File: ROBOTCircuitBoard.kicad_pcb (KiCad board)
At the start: 2 copper layers, 52.1 x 74.9 mm, 13 parts, among them J1 DB15_HighDensity_MountingHoles, J2 DB15_HighDensity_MountingHoles, P1 CONN_01X03, P2 CONN_01X04, P3 CONN_01X04, P4 CONN_01X04, U1 MCP2551-I/P, U2 Teensy3.2

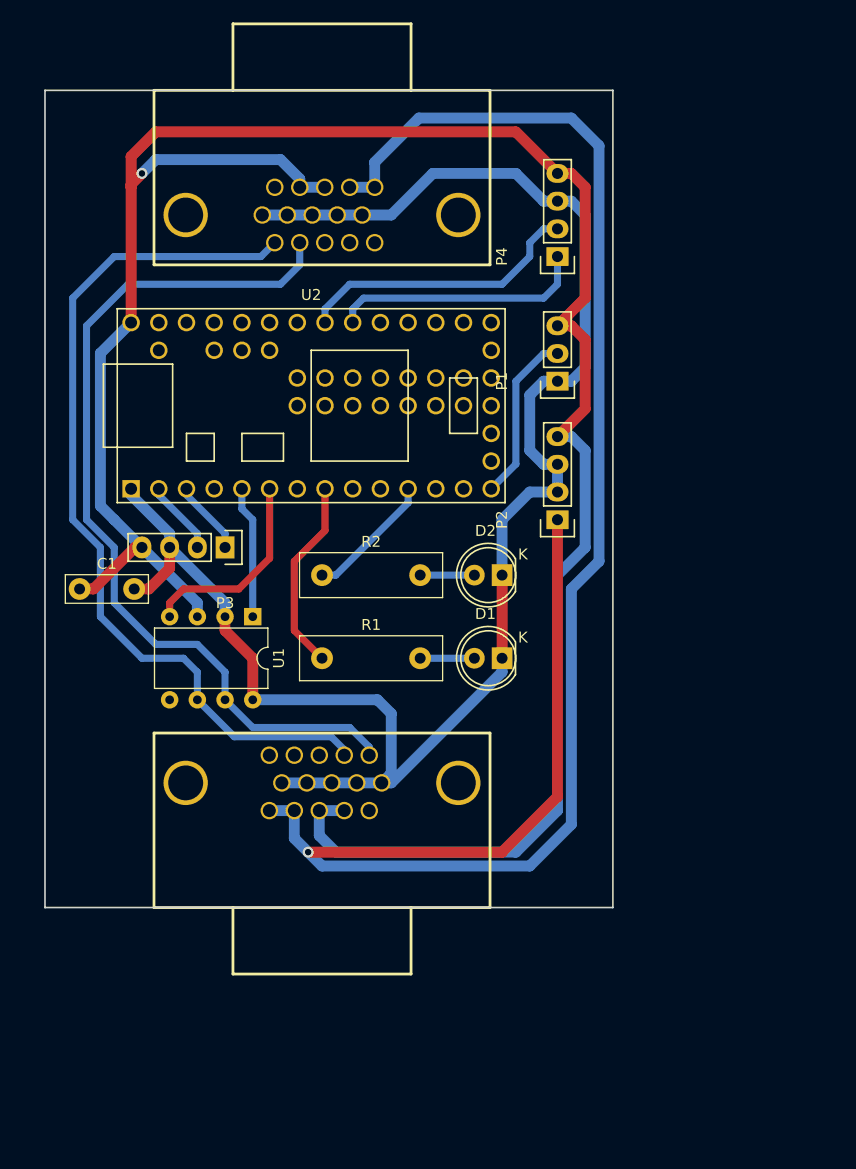
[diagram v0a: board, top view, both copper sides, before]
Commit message: Added four pin connectors, 5V layer, GND layer, and other misceallaneous jobs.
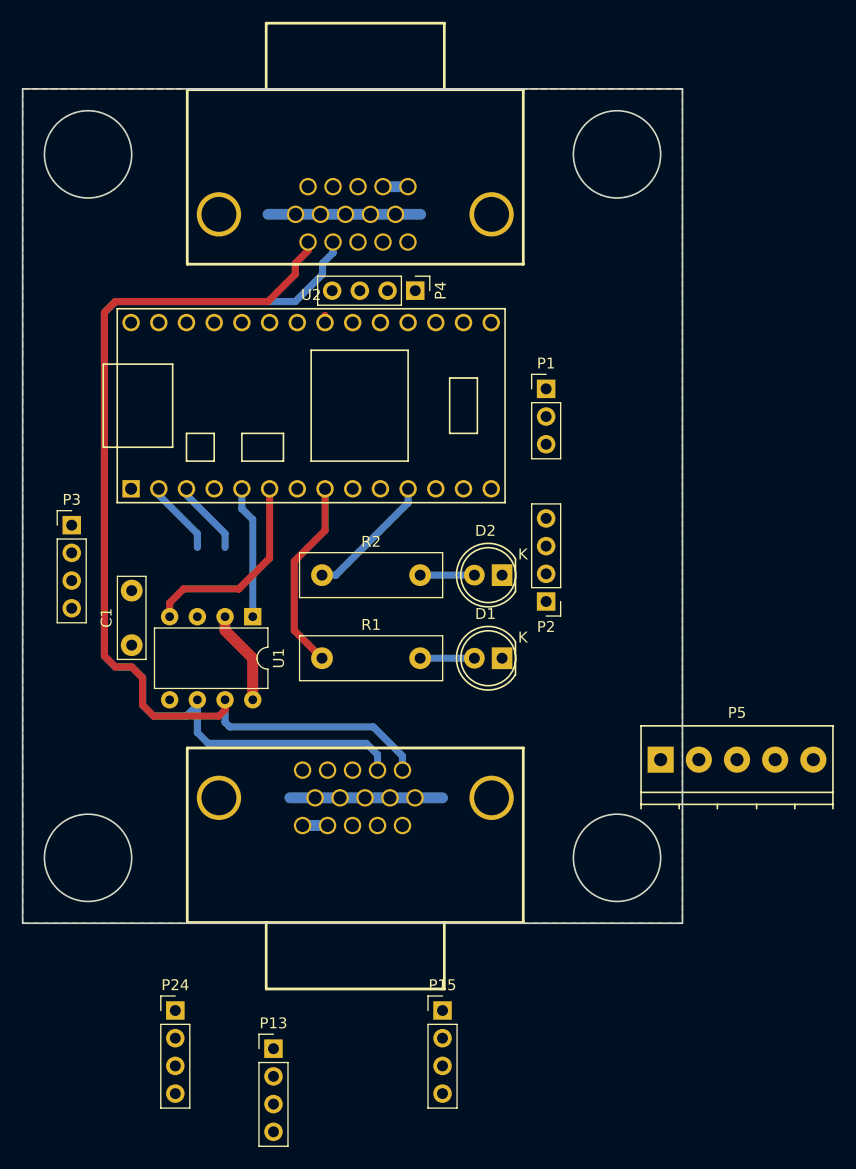
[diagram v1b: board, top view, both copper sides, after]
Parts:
- added P13: CONN_01X04, Socket_Strips:Socket_Strip_Straight_1x04_Pitch2.54mm, F.Cu at (167.0, 175.5)
- added P15: CONN_01X04, Socket_Strips:Socket_Strip_Straight_1x04_Pitch2.54mm, F.Cu at (182.5, 172.0)
- added P24: CONN_01X04, Socket_Strips:Socket_Strip_Straight_1x04_Pitch2.54mm, F.Cu at (158.0, 172.0)
- added P5: CONN_01X05, Connectors_Terminal_Blocks:TerminalBlock_Pheonix_PT-3.5mm_5pol, F.Cu at (202.5, 149.0)
- P1: footprint Socket_Strips:Socket_Strip_Straight_1x03 -> Socket_Strips:Socket_Strip_Straight_1x03_Pitch2.54mm
- P2, P3, P4: footprint Socket_Strips:Socket_Strip_Straight_1x04 -> Socket_Strips:Socket_Strip_Straight_1x04_Pitch2.54mm
- U2: footprint Teensy:Teensy30_31_32_LC -> Teensy:Teensy30_31_32_LC_LessPins
- moved P3 14.2 mm to (148.5, 127.5), turned to 0 degrees
- moved P4 13.4 mm to (180.0, 106.0), turned to 270 degrees
- moved P2 7.57 mm to (192.0, 134.5), turned to 180 degrees
- moved C1 7.02 mm to (154.0, 138.5), turned to 90 degrees
- moved J1 3.34 mm to (174.5, 152.5)
- moved J2 3.05 mm to (174.5, 99.0)
- moved P1 1.25 mm to (192.0, 115.0), turned to 0 degrees
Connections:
- J2 pad 1: /CANL -> /CANH
- J2 pad 2: /CANH -> /CANL
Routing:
- net +5V: track 212.0 -> 0.02 mm, vias 1 -> 0
- net +12V: track 174.6 -> 4.58 mm, vias 1 -> 0
- net GND: track 157.9 -> 36.7 mm
- net /1B: track 26.4 -> 0.67 mm
- net /1A: track 23.5 -> 0.00 mm
- net /DIN: track 15.7 -> 0.00 mm
- net /CANL: track 80.3 -> 91.2 mm
- net /CANH: track 81.4 -> 90.8 mm
- net Net-(J1-Pad0): track 1.47 -> 0.00 mm
- added copper zone on F.Cu, net +5V
- added copper zone on B.Cu, net GND
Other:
- board size 52.1 x 74.9 mm -> 60.5 x 76.5 mm

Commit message: added some 5v GND DATA DATA ports. Repositioned Pololu. Reduced board size slightly
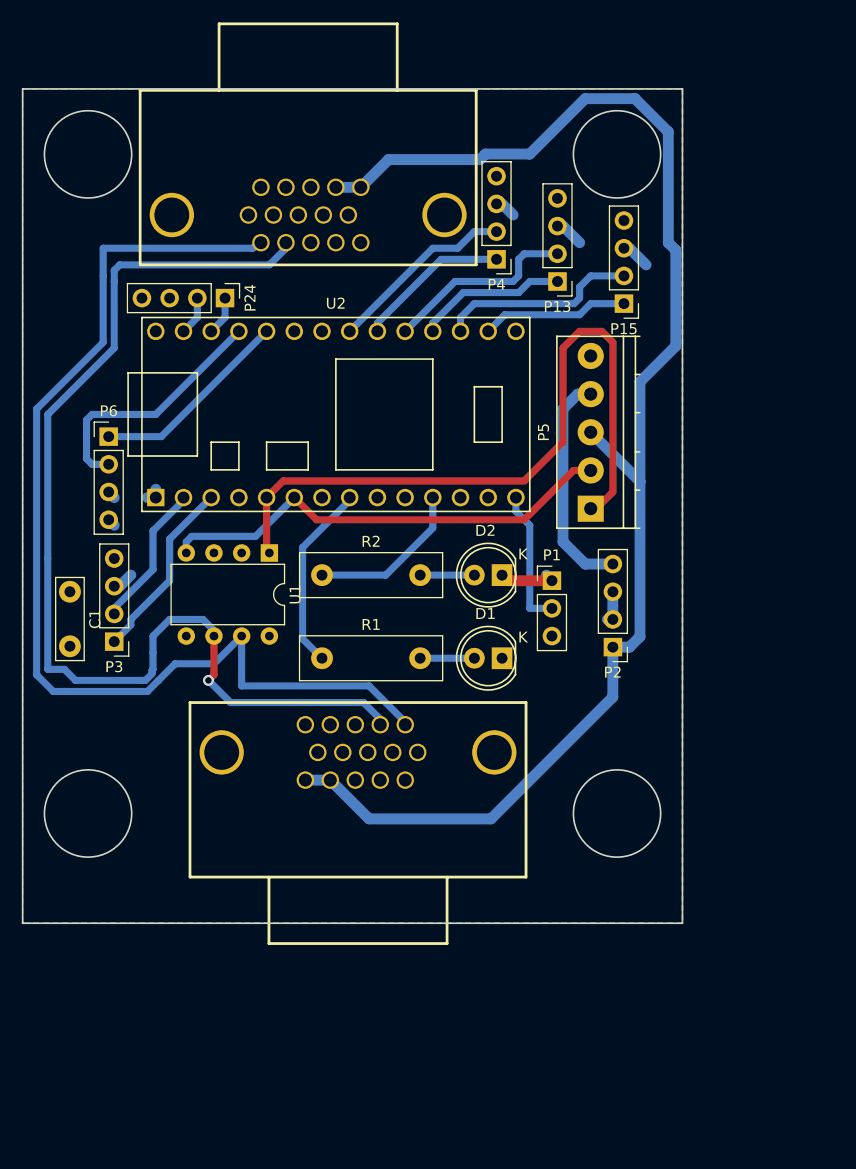
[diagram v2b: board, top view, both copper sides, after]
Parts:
- added P6: CONN_01X04, Socket_Strips:Socket_Strip_Straight_1x04_Pitch2.54mm, F.Cu at (151.9, 119.4)
- moved P13 75.0 mm to (193.0, 105.2), turned to 180 degrees
- moved P15 66.9 mm to (199.1, 107.2), turned to 180 degrees
- moved P24 65.5 mm to (162.6, 106.7), turned to 270 degrees
- moved P5 23.9 mm to (196.1, 126.0), turned to 90 degrees
- moved P1 17.6 mm to (192.5, 132.6)
- moved P3 11.4 mm to (152.4, 138.2), turned to 180 degrees
- moved P4 7.99 mm to (187.5, 103.1), turned to 180 degrees
- moved C1 7.49 mm to (148.3, 133.6), turned to 270 degrees
- moved P2 7.41 mm to (198.1, 138.7)
- moved U1 6.04 mm to (166.6, 130.0)
- moved J2 4.32 mm to (170.2, 99.1)
- moved J1 4.17 mm to (174.8, 148.3)
- moved U2 2.40 mm to (172.7, 117.3)
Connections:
- net Net-(U2-Pad27) renamed /A4
- net Net-(U2-Pad28) renamed /A5
- P13 pad 1: Net-(P13-Pad1) -> /A2
- P13 pad 2: Net-(P13-Pad2) -> /A3
- P13 pad 3: Net-(P13-Pad3) -> GND
- P13 pad 4: Net-(P13-Pad4) -> +5V
- P15 pad 1: Net-(P15-Pad1) -> /A0
- P15 pad 2: Net-(P15-Pad2) -> /A1
- P15 pad 3: Net-(P15-Pad3) -> GND
- P15 pad 4: Net-(P15-Pad4) -> +5V
- P24 pad 1: Net-(P24-Pad1) -> /A8
- P24 pad 2: Net-(P24-Pad2) -> /A9
- P24 pad 3: Net-(P24-Pad3) -> GND
- P24 pad 4: Net-(P24-Pad4) -> +5V
- P5 pad 1: Net-(P5-Pad1) -> /CAN_Tx
- P5 pad 2: Net-(P5-Pad2) -> /CAN_Rx
- P5 pad 3: Net-(P5-Pad3) -> +12V
- P5 pad 4: Net-(P5-Pad4) -> +5V
- P5 pad 5: Net-(P5-Pad5) -> GND
- U2 pad 21: Net-(U2-Pad21) -> /A0
- U2 pad 22: Net-(U2-Pad22) -> /A1
- U2 pad 23: Net-(U2-Pad23) -> /A2
- U2 pad 24: Net-(U2-Pad24) -> /A3
- U2 pad 29: Net-(U2-Pad29) -> /A6
- U2 pad 30: Net-(U2-Pad30) -> /A7
- U2 pad 31: Net-(U2-Pad31) -> /A8
- U2 pad 32: Net-(U2-Pad32) -> /A9
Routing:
- net +12V: track 4.58 -> 131.2 mm
- net /CAN_Tx: track 12.1 -> 65.1 mm
- net /CAN_Rx: track 18.5 -> 42.5 mm
- net /A7: track 0.00 -> 23.1 mm
- net +5V: track 0.02 -> 22.1 mm
- net /A6: track 0.00 -> 18.5 mm
- net /A1: track 0.00 -> 18.4 mm
- net /A3: track 0.00 -> 17.8 mm
- net /1B: track 0.67 -> 17.2 mm
- net GND: track 36.7 -> 20.9 mm
- net /1A: track 0.00 -> 14.1 mm
- net /A2: track 0.00 -> 13.8 mm
- net /A0: track 0.00 -> 13.5 mm
- net /DIN: track 0.00 -> 12.7 mm
- net /0B: track 6.84 -> 16.9 mm
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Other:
- outline, holes or cut-outs redrawn

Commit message: fixed board size
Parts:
- moved J1 4.06 mm to (174.8, 152.4)
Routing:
- net /CANL: track 99.1 -> 103.1 mm
- net /CANH: track 99.3 -> 103.4 mm
- net +12V: track 131.2 -> 134.3 mm
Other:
- outline, holes or cut-outs redrawn
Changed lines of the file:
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@@
     (links 72)
     (no_connects 2)
-    (area 143.924999 87.424999 204.575001 164.075001)
+    (area 143.924999 81.206999 204.592004 166.189001)
     (thickness 1.6)
     (drawings 8)
-    (tracks 180)
+    (tracks 183)
     (zones 0)
     (modules 18)
@@
   )
   (module conn-db15-SPC15430:conn_SPC15430 (layer F.Cu)
-    (at 174.752 148.336 180)
+    (at 174.752 152.4 180)
     (fp_text reference J1 (at -8.6487 -6.9088 180) (layer F.SilkS) hide
       (effects (font (size 0.59944 0.59944) (thickness 0.0508)))
@@
   (gr_line (start 204.5 164) (end 144 164) (angle 90) (layer Edge.Cuts) (width 0.15))
   (gr_line (start 204.5 87.5) (end 204.5 164) (angle 90) (layer Edge.Cuts) (width 0.15))
-  (gr_circle (center 150 153.936) (end 154 153.936) (layer Edge.Cuts) (width 0.15))
-  (gr_circle (center 198.5 153.936) (end 194.5 153.936) (layer Edge.Cuts) (width 0.15))
+  (gr_circle (center 149.492 157.492) (end 153.492 157.492) (layer Edge.Cuts) (width 0.15))
+  (gr_circle (center 198.5 158) (end 194.5 158) (layer Edge.Cuts) (width 0.15))
   (gr_circle (center 198.5 93.5) (end 194.5 93.5) (layer Edge.Cuts) (width 0.15))
   (gr_circle (center 150 93.5) (end 154 93.5) (layer Edge.Cuts) (width 0.15))
@@
   (segment (start 180.45 139.7) (end 185.42 139.7) (width 0.65) (layer B.Cu) (net 2))
   (segment (start 180.45 132.08) (end 185.42 132.08) (width 0.65) (layer B.Cu) (net 3))
-  (segment (start 198.12 138.684) (end 198.12 143.256) (width 1) (layer B.Cu) (net 5))
-  (segment (start 175.768 154.432) (end 172.212 150.876) (width 1) (layer B.Cu) (net 5))
-  (segment (start 186.944 154.432) (end 175.768 154.432) (width 1) (layer B.Cu) (net 5))
-  (segment (start 198.12 143.256) (end 186.944 154.432) (width 1) (layer B.Cu) (net 5))
-  (segment (start 169.922 150.876) (end 172.212 150.876) (width 1) (layer B.Cu) (net 5))
+  (segment (start 172.212 154.94) (end 172.212 155.956) (width 1) (layer B.Cu) (net 5) (status 400000))
+  (segment (start 198.12 146.812) (end 198.12 138.684) (width 1) (layer B.Cu) (net 5) (status 800000))
+  (segment (start 187.96 156.972) (end 198.12 146.812) (width 1) (layer B.Cu) (net 5))
+  (segment (start 173.228 156.972) (end 187.96 156.972) (width 1) (layer B.Cu) (net 5))
+  (segment (start 172.212 155.956) (end 173.228 156.972) (width 1) (layer B.Cu) (net 5))
+  (segment (start 172.212 154.94) (end 169.922 154.94) (width 1) (layer B.Cu) (net 5) (status C00000))
   (segment (start 198.12 138.684) (end 199.644 138.684) (width 1) (layer B.Cu) (net 5))
+  (segment (start 200.604 137.724) (end 200.604 123.5) (width 1) (layer B.Cu) (net 5))
   (segment (start 199.644 138.684) (end 200.604 137.724) (width 1) (layer B.Cu) (net 5))
-  (segment (start 200.604 137.724) (end 200.604 123.5) (width 1) (layer B.Cu) (net 5))
   (segment (start 200.604 123.5) (end 200.604 114.356) (width 1) (layer B.Cu) (net 5))
   (segment (start 177.55 93.98) (end 175.01 96.52) (width 1) (layer B.Cu) (net 5))
@@
   (segment (start 152.4 127.508) (end 151.892 127) (width 1) (layer B.Cu) (net 6))
   (segment (start 148.844 133.604) (end 148.336 133.604) (width 1) (layer B.Cu) (net 6))
+  (segment (start 179.082 149.86) (end 179.082 145.796) (width 0.65) (layer B.Cu) (net 11) (status 400000))
+  (segment (start 164.084 142.24) (end 164.084 137.668) (width 0.65) (layer B.Cu) (net 11))
+  (segment (start 175.768 142.24) (end 164.084 142.24) (width 0.65) (layer B.Cu) (net 11))
+  (segment (start 179.082 145.554) (end 175.768 142.24) (width 0.65) (layer B.Cu) (net 11))
+  (segment (start 179.082 145.796) (end 179.082 145.554) (width 0.65) (layer B.Cu) (net 11))
   (segment (start 151.384 104.648) (end 151.384 102.108) (width 0.65) (layer B.Cu) (net 11))
   (segment (start 146.812 142.748) (end 155.448 142.748) (width 0.65) (layer B.Cu) (net 11))
@@
   (segment (start 151.384 102.108) (end 165.1 102.108) (width 0.65) (layer B.Cu) (net 11))
   (segment (start 165.608 101.6) (end 165.85 101.6) (width 0.65) (layer B.Cu) (net 11))
-  (segment (start 179.082 145.796) (end 179.082 145.554) (width 0.65) (layer B.Cu) (net 11))
-  (segment (start 179.082 145.554) (end 175.768 142.24) (width 0.65) (layer B.Cu) (net 11))
-  (segment (start 175.768 142.24) (end 164.084 142.24) (width 0.65) (layer B.Cu) (net 11))
-  (segment (start 164.084 142.24) (end 164.084 137.668) (width 0.65) (layer B.Cu) (net 11))
   (segment (start 165.85 101.6) (end 165.85 101.866) (width 0.65) (layer B.Cu) (net 11))
+  (segment (start 176.792 149.86) (end 176.792 145.796) (width 0.65) (layer B.Cu) (net 12) (status 400000))
+  (segment (start 161.544 141.224) (end 161.544 137.668) (width 0.65) (layer F.Cu) (net 12))
+  (segment (start 161.036 141.732) (end 161.544 141.224) (width 0.65) (layer F.Cu) (net 12))
+  (via (at 161.036 141.732) (size 1) (drill 0.6) (layers F.Cu B.Cu) (net 12))
+  (segment (start 163.068 143.764) (end 161.036 141.732) (width 0.65) (layer B.Cu) (net 12))
+  (segment (start 175.26 143.764) (end 163.068 143.764) (width 0.65) (layer B.Cu) (net 12))
+  (segment (start 176.792 145.296) (end 175.26 143.764) (width 0.65) (layer B.Cu) (net 12))
+  (segment (start 176.792 145.796) (end 176.792 145.296) (width 0.65) (layer B.Cu) (net 12))
   (segment (start 168.14 101.6) (end 168.14 102.116) (width 0.65) (layer B.Cu) (net 12))
   (segment (start 168.14 102.116) (end 166.624 103.632) (width 0.65) (layer B.Cu) (net 12))
@@
   (segment (start 155.956 140.716) (end 155.862958 140.809042) (width 0.65) (layer B.Cu) (net 12))
   (segment (start 154.94 141.732) (end 155.261916 141.732) (width 0.65) (layer B.Cu) (net 12))
-  (segment (start 176.792 145.796) (end 176.792 145.296) (width 0.65) (layer B.Cu) (net 12))
-  (segment (start 176.792 145.296) (end 175.26 143.764) (width 0.65) (layer B.Cu) (net 12))
-  (segment (start 175.26 143.764) (end 163.068 143.764) (width 0.65) (layer B.Cu) (net 12))
-  (segment (start 163.068 143.764) (end 161.036 141.732) (width 0.65) (layer B.Cu) (net 12))
-  (via (at 161.036 141.732) (size 1) (drill 0.6) (layers F.Cu B.Cu) (net 12))
-  (segment (start 161.036 141.732) (end 161.544 141.224) (width 0.65) (layer F.Cu) (net 12))
-  (segment (start 161.544 141.224) (end 161.544 137.668) (width 0.65) (layer F.Cu) (net 12))
   (segment (start 161.544 137.16) (end 161.544 137.668) (width 0.65) (layer B.Cu) (net 12))
   (segment (start 192.532 135.128) (end 190.5 135.128) (width 0.65) (layer B.Cu) (net 18))

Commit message: added name and number
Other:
- board text added: "BP 0203"
- board text added: "Bot Provoking"
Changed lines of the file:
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@@
     (links 72)
     (no_connects 2)
-    (area 143.924999 81.206999 204.592004 166.189001)
+    (area 143.924999 81.206999 204.592004 170.253001)
     (thickness 1.6)
-    (drawings 8)
+    (drawings 10)
     (tracks 183)
     (zones 0)
@@
     )
   )
+  (gr_text "Bot Provoking" (at 153.924 148.336) (layer B.SilkS)
+    (effects (font (size 1.5 1.5) (thickness 0.3)))
+  )
+  (gr_text "BP 0203" (at 150.876 145.796) (layer B.SilkS)
+    (effects (font (size 1.5 1.5) (thickness 0.3)))
+  )
   (gr_line (start 144 87.5) (end 144 164) (angle 90) (layer Edge.Cuts) (width 0.15))
   (gr_line (start 144 87.5) (end 204.5 87.5) (angle 90) (layer Edge.Cuts) (width 0.15))
@@
   (segment (start 180.45 139.7) (end 185.42 139.7) (width 0.65) (layer B.Cu) (net 2))
   (segment (start 180.45 132.08) (end 185.42 132.08) (width 0.65) (layer B.Cu) (net 3))
-  (segment (start 172.212 154.94) (end 172.212 155.956) (width 1) (layer B.Cu) (net 5) (status 400000))
-  (segment (start 198.12 146.812) (end 198.12 138.684) (width 1) (layer B.Cu) (net 5) (status 800000))
+  (segment (start 172.212 154.94) (end 172.212 155.956) (width 1) (layer B.Cu) (net 5))
+  (segment (start 198.12 146.812) (end 198.12 138.684) (width 1) (layer B.Cu) (net 5))
   (segment (start 187.96 156.972) (end 198.12 146.812) (width 1) (layer B.Cu) (net 5))
   (segment (start 173.228 156.972) (end 187.96 156.972) (width 1) (layer B.Cu) (net 5))
   (segment (start 172.212 155.956) (end 173.228 156.972) (width 1) (layer B.Cu) (net 5))
-  (segment (start 172.212 154.94) (end 169.922 154.94) (width 1) (layer B.Cu) (net 5) (status C00000))
+  (segment (start 172.212 154.94) (end 169.922 154.94) (width 1) (layer B.Cu) (net 5))
   (segment (start 198.12 138.684) (end 199.644 138.684) (width 1) (layer B.Cu) (net 5))
   (segment (start 200.604 137.724) (end 200.604 123.5) (width 1) (layer B.Cu) (net 5))
@@
   (segment (start 152.4 127.508) (end 151.892 127) (width 1) (layer B.Cu) (net 6))
   (segment (start 148.844 133.604) (end 148.336 133.604) (width 1) (layer B.Cu) (net 6))
-  (segment (start 179.082 149.86) (end 179.082 145.796) (width 0.65) (layer B.Cu) (net 11) (status 400000))
+  (segment (start 179.082 149.86) (end 179.082 145.796) (width 0.65) (layer B.Cu) (net 11))
   (segment (start 164.084 142.24) (end 164.084 137.668) (width 0.65) (layer B.Cu) (net 11))
   (segment (start 175.768 142.24) (end 164.084 142.24) (width 0.65) (layer B.Cu) (net 11))
@@
   (segment (start 165.608 101.6) (end 165.85 101.6) (width 0.65) (layer B.Cu) (net 11))
   (segment (start 165.85 101.6) (end 165.85 101.866) (width 0.65) (layer B.Cu) (net 11))
-  (segment (start 176.792 149.86) (end 176.792 145.796) (width 0.65) (layer B.Cu) (net 12) (status 400000))
+  (segment (start 176.792 149.86) (end 176.792 145.796) (width 0.65) (layer B.Cu) (net 12))
   (segment (start 161.544 141.224) (end 161.544 137.668) (width 0.65) (layer F.Cu) (net 12))
   (segment (start 161.036 141.732) (end 161.544 141.224) (width 0.65) (layer F.Cu) (net 12))
